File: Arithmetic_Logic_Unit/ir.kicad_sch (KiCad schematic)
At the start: 19 parts, among them IC1 SN54173J, IC2 SN54173J, U1 74LS245

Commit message: added instructional register
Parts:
- removed D1, D2, D3, D4, D5, D6, D7, D8: LED, symbol Device:LED
- removed IC1, IC2: SN54173J, footprints:SN54173J, symbol SN54173J:SN54173J
- removed R1, R2, R3, R4, R5, R6, R7, R8: 220, symbol Device:R
- removed U1: 74LS245, symbol 74xx:74LS245
- added D25, D26, D27, D28, D29, D30, D31, D32: LED, symbol Device:LED
- added IC5, IC6: SN54173J, footprints:SN54173J, symbol SN54173J:SN54173J
- added R25, R26, R27, R28, R29, R30, R31, R32: 220, symbol Device:R
- added U8: 74LS245, symbol 74xx:74LS245
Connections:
- net 5V: now also IC5.16 (VCC), IC6.16 (VCC), U8.1 (A->B), U8.20 (VCC)
- net GND: now also IC5.8 (GND), IC6.8 (GND), R25.2, R26.2, R27.2, R28.2, R29.2, R30.2, R31.2, R32.2, U8.10 (GND)
- net bus0: now also IC5.14 (1D), U8.18 (B0)
- net bus1: now also IC5.13 (2D), U8.17 (B1)
- net bus2: now also IC5.12 (3D), U8.16 (B2)
- net bus3: now also IC5.11 (4D), U8.15 (B3)
- net bus4: now also IC6.14 (1D), U8.14 (B4)
- net bus5: now also IC6.13 (2D), U8.13 (B5)
- net bus6: now also IC6.12 (3D), U8.12 (B6)
- net bus7: now also IC6.11 (4D), U8.11 (B7)
- net clear: now also IC5.15 (CLR), IC6.15 (CLR)
- net clock: now also IC5.7 (CLK), IC6.7 (CLK)
- net enable: now also IC5.1 (M), IC5.2 (N), IC6.1 (M), IC6.2 (N)
- net load: now also IC5.10 (~{G2}), IC5.9 (~{G1}), IC6.10 (~{G2}), IC6.9 (~{G1})
- net q0: now also D25.2 (A), IC5.3 (1Q)
- net q1: now also D26.2 (A), IC5.4 (2Q)
- net q2: now also D27.2 (A), IC5.5 (3Q)
- net q3: now also D28.2 (A), IC5.6 (4Q)
- net q4: now also D29.2 (A), IC6.3 (1Q), U8.6 (A4)
- net q5: now also D30.2 (A), IC6.4 (2Q), U8.7 (A5)
- net q6: now also D31.2 (A), IC6.5 (3Q), U8.8 (A6)
- net q7: now also D32.2 (A), IC6.6 (4Q), U8.9 (A7)
- net ~{OE}: now also U8.19 (CE)
- new net: D29.1 (K), R29.1
- new net: D32.1 (K), R32.1
- new net: D30.1 (K), R30.1
- new net: D28.1 (K), R28.1
- new net: D27.1 (K), R27.1
- new net: D25.1 (K), R25.1
- new net: D26.1 (K), R26.1
- new net: D31.1 (K), R31.1
- no-connect marks 0 -> 4
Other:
- title: Registers -> (none)

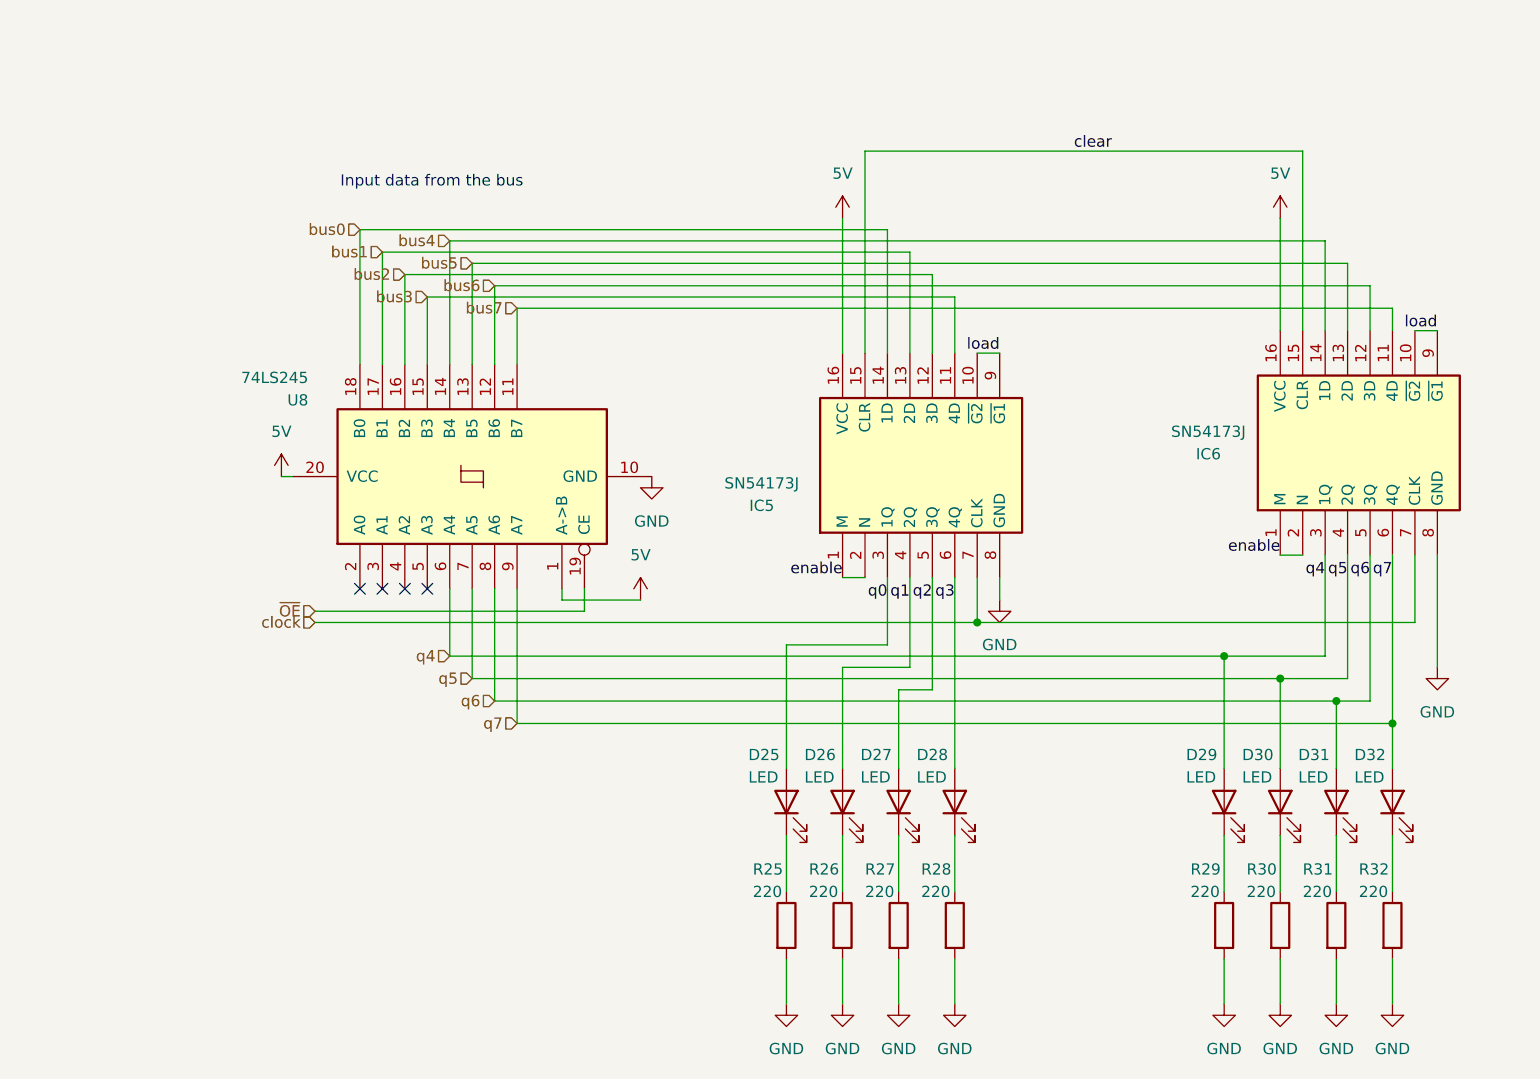
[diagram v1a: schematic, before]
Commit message: fixed incorrect footprint for sn54173
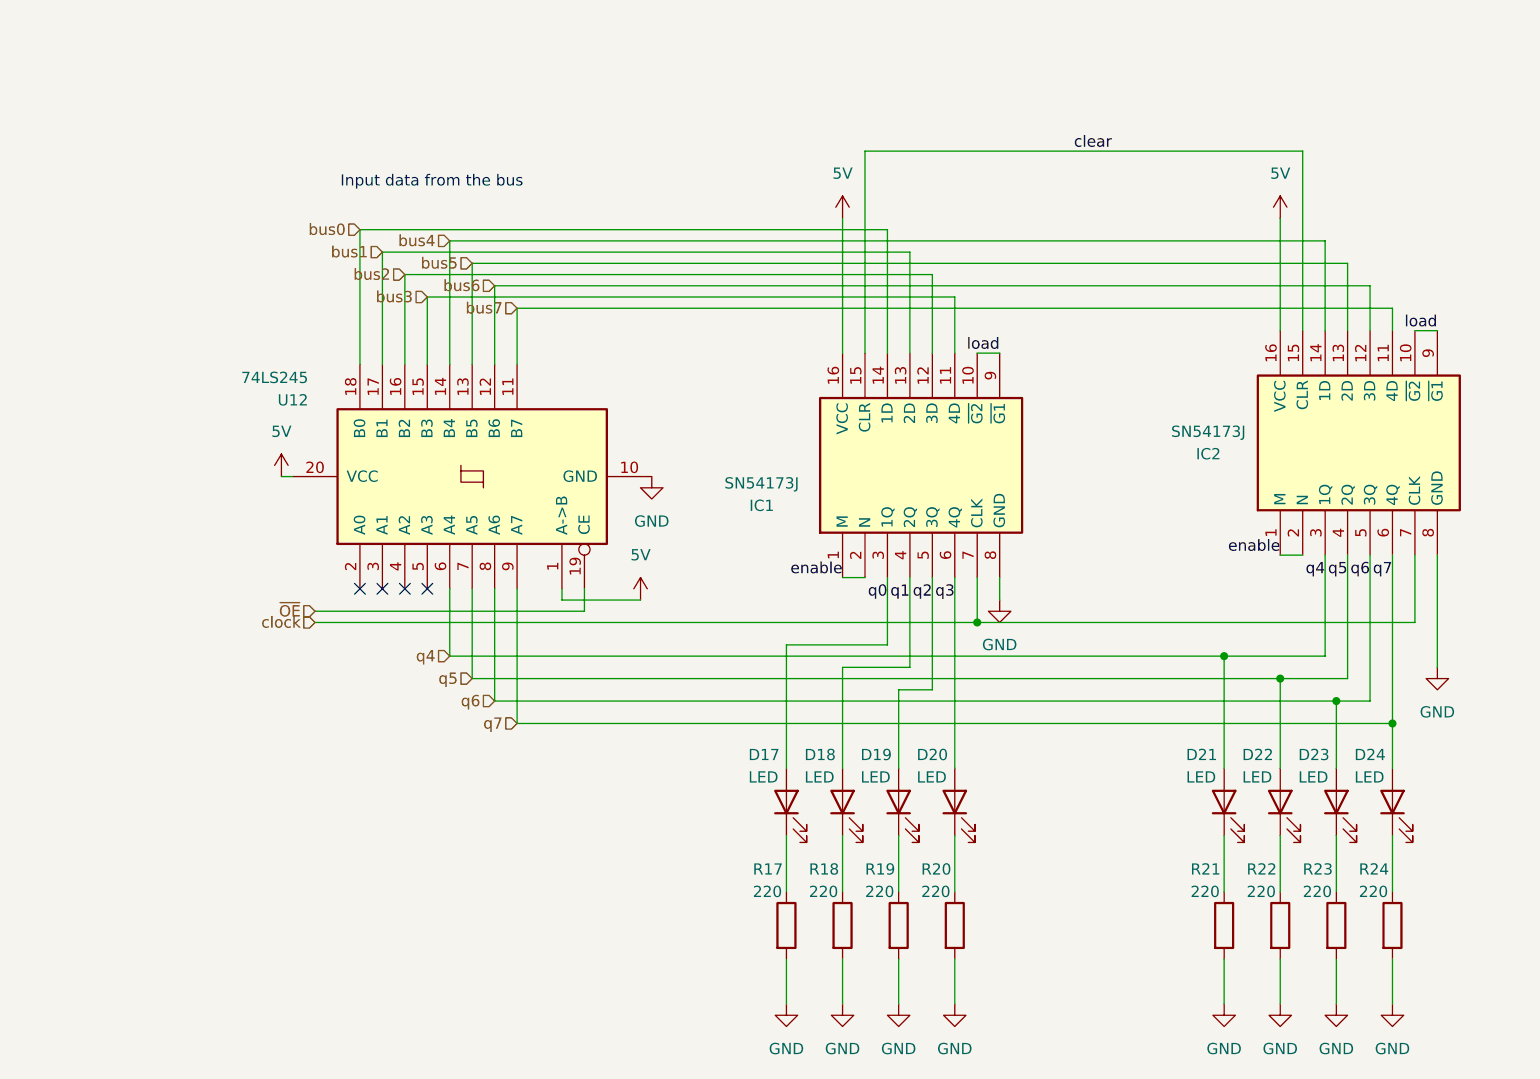
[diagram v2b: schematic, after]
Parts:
- renumbered D25 to D17, D26 to D18, D27 to D19, D28 to D20, D29 to D21, D30 to D22, D31 to D23, D32 to D24, IC5 to IC1, IC6 to IC2, R25 to R17, R26 to R18, R27 to R19, R28 to R20, R29 to R21, R30 to R22, R31 to R23, R32 to R24, U8 to U12

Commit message: added bypass capacitors
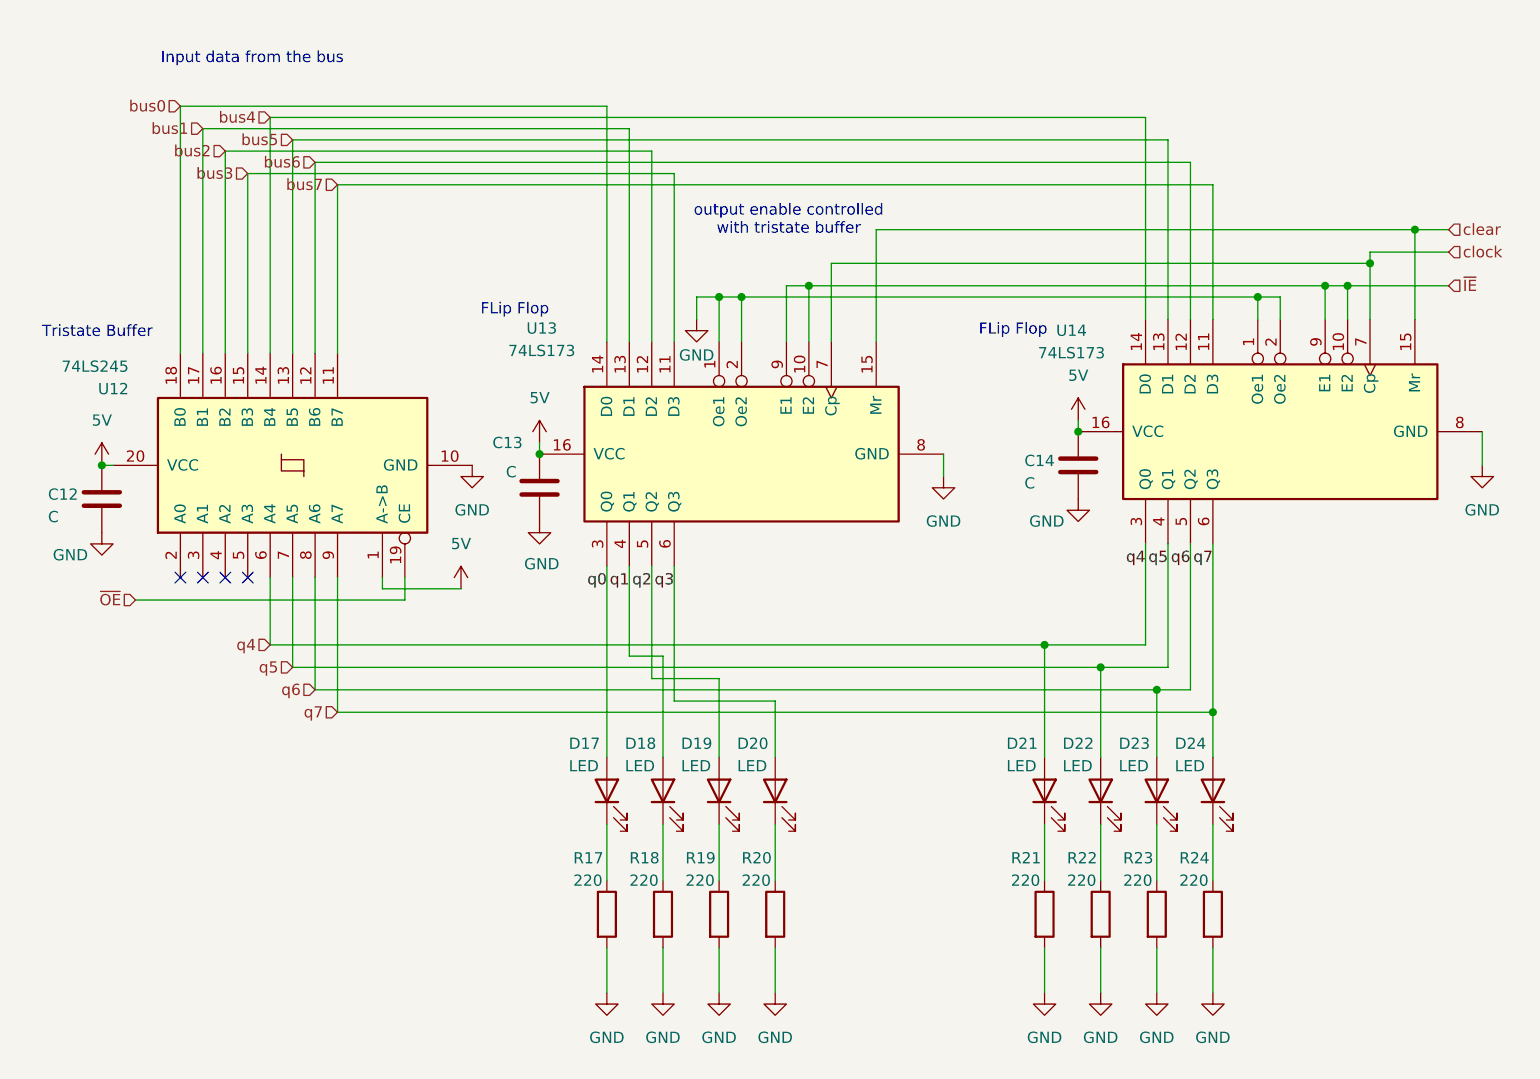
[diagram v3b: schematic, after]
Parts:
- removed IC1, IC2: SN54173J, footprints:SN54173J, symbol SN54173J:SN54173J
- added C12, C13, C14: C, symbol Device:C
- added U13, U14: 74LS173, symbol 74xx:74LS173
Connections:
- net 5V: now also C12.2, C13.2, C14.2, U13.16 (VCC), U14.16 (VCC)
- net GND: now also C12.1, C13.1, C14.1, U13.1 (Oe1), U13.2 (Oe2), U13.8 (GND), U14.1 (Oe1), U14.2 (Oe2), U14.8 (GND)
- net bus0: now also U13.14 (D0)
- net bus1: now also U13.13 (D1)
- net bus2: now also U13.12 (D2)
- net bus3: now also U13.11 (D3)
- net bus4: now also U14.14 (D0)
- net bus5: now also U14.13 (D1)
- net bus6: now also U14.12 (D2)
- net bus7: now also U14.11 (D3)
- net clear: now also U13.15 (Mr), U14.15 (Mr)
- net clock: now also U13.7 (Cp), U14.7 (Cp)
- net q0: now also U13.3 (Q0)
- net q1: now also U13.4 (Q1)
- net q2: now also U13.5 (Q2)
- net q3: now also U13.6 (Q3)
- net q4: now also U14.3 (Q0)
- net q5: now also U14.4 (Q1)
- net q6: now also U14.5 (Q2)
- net q7: now also U14.6 (Q3)
- new net ~{IE}: U13.10 (E2), U13.9 (E1), U14.10 (E2), U14.9 (E1)
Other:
- note added: "FLip Flop"
- note added: "Tristate Buffer"
- note added: "output enable controlled with tristate buffer"

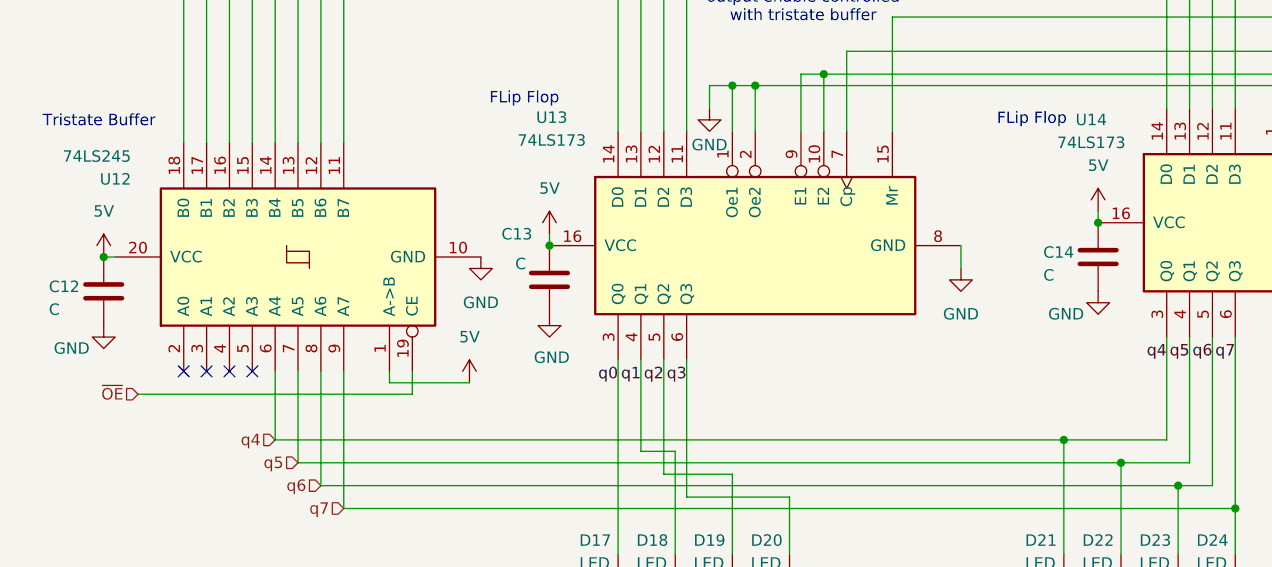
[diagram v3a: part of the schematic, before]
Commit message: preliminary board layout, will move IR to clock module
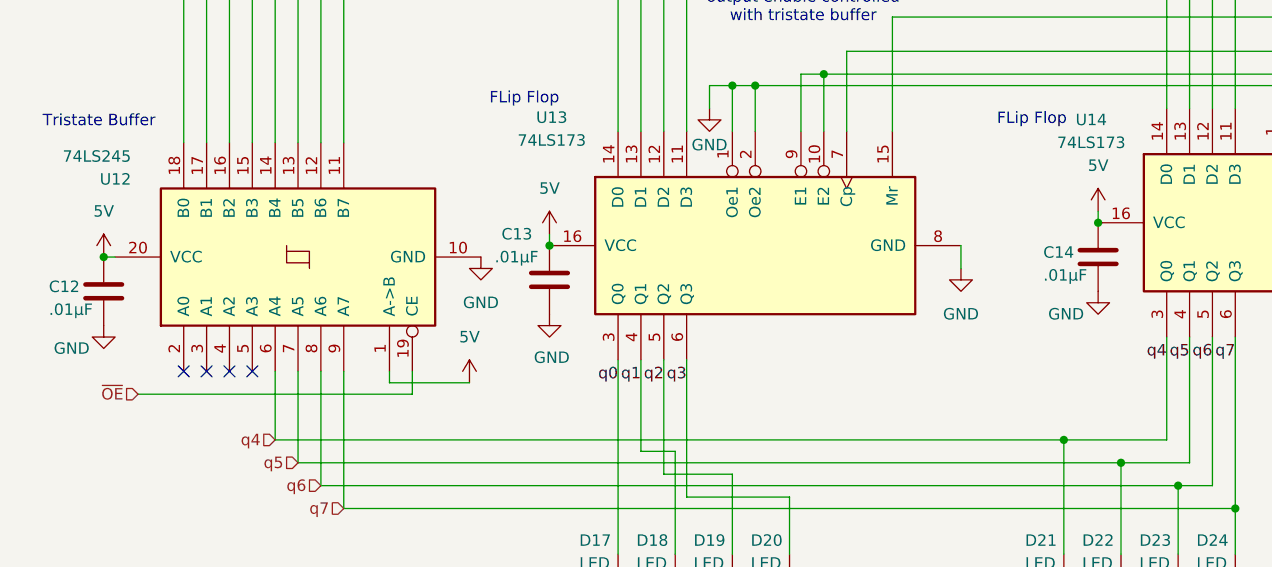
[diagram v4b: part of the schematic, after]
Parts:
- C12, C13, C14: value C -> .01µF; footprint (none) -> Capacitor_THT:C_Disc_D5.0mm_W2.5mm_P2.50mm
- D17, D18, D19, D20, D21, D22, D23, D24: footprint (none) -> LED_THT:LED_D5.0mm
- R17, R18, R19, R20, R21, R22, R23, R24: footprint (none) -> Resistor_THT:R_Axial_DIN0207_L6.3mm_D2.5mm_P5.08mm_Vertical
- U12: footprint (none) -> Package_DIP:DIP-20_W7.62mm
- U13, U14: footprint (none) -> Package_DIP:DIP-16_W7.62mm
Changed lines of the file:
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@@
 			)
 		)
-		(property "Footprint" ""
+		(property "Footprint" "Resistor_THT:R_Axial_DIN0207_L6.3mm_D2.5mm_P5.08mm_Vertical"
 			(at 151.892 123.19 90)
 			(effects
@@
 			)
 		)
-		(property "Footprint" ""
+		(property "Footprint" "Package_DIP:DIP-16_W7.62mm"
 			(at 167.64 68.58 0)
 			(effects
@@
 			)
 		)
-		(property "Footprint" ""
+		(property "Footprint" "Package_DIP:DIP-16_W7.62mm"
 			(at 106.68 71.12 0)
 			(effects
@@
 			)
 		)
-		(property "Value" "C"
+		(property "Value" ".01µF"
 			(at 28.194 78.232 0)
 			(effects
@@
 			)
 		)
-		(property "Footprint" ""
+		(property "Footprint" "Capacitor_THT:C_Disc_D5.0mm_W2.5mm_P2.50mm"
 			(at 33.3248 72.39 0)
 			(effects
@@
 			)
 		)
-		(property "Footprint" ""
+		(property "Footprint" "Resistor_THT:R_Axial_DIN0207_L6.3mm_D2.5mm_P5.08mm_Vertical"
 			(at 139.192 123.19 90)
 			(effects
@@
 			)
 		)
-		(property "Value" "C"
+		(property "Value" ".01µF"
 			(at 138.684 74.422 0)
 			(effects
@@
 			)
 		)
-		(property "Footprint" ""
+		(property "Footprint" "Capacitor_THT:C_Disc_D5.0mm_W2.5mm_P2.50mm"
 			(at 143.8148 68.58 0)
 			(effects
@@
 			)
 		)
-		(property "Footprint" ""
+		(property "Footprint" "LED_THT:LED_D5.0mm"
 			(at 147.32 109.22 0)
 			(effects
@@
 			)
 		)
-		(property "Footprint" ""
+		(property "Footprint" "LED_THT:LED_D5.0mm"
 			(at 104.14 109.22 0)
 			(effects
@@
 			)
 		)
-		(property "Footprint" ""
+		(property "Footprint" "LED_THT:LED_D5.0mm"
 			(at 110.49 109.22 0)
 			(effects
@@
 			)
 		)
-		(property "Footprint" ""
+		(property "Footprint" "Resistor_THT:R_Axial_DIN0207_L6.3mm_D2.5mm_P5.08mm_Vertical"
 			(at 102.362 123.19 90)
 			(effects
@@
 			)
 		)
-		(property "Footprint" ""
+		(property "Footprint" "Resistor_THT:R_Axial_DIN0207_L6.3mm_D2.5mm_P5.08mm_Vertical"
 			(at 108.712 123.19 90)
 			(effects
@@
 			)
 		)
-		(property "Footprint" ""
+		(property "Footprint" "LED_THT:LED_D5.0mm"
 			(at 91.44 109.22 0)
 			(effects
@@
 			)
 		)
-		(property "Footprint" ""
+		(property "Footprint" "LED_THT:LED_D5.0mm"
 			(at 153.67 109.22 0)
 			(effects
@@
 			)
 		)
-		(property "Footprint" ""
+		(property "Footprint" "Resistor_THT:R_Axial_DIN0207_L6.3mm_D2.5mm_P5.08mm_Vertical"
 			(at 96.012 123.19 90)
 			(effects
@@
 			)
 		)
-		(property "Footprint" ""
+		(property "Footprint" "LED_THT:LED_D5.0mm"
 			(at 97.79 109.22 0)
 			(effects
@@
 			)
 		)
-		(property "Footprint" ""
+		(property "Footprint" "Resistor_THT:R_Axial_DIN0207_L6.3mm_D2.5mm_P5.08mm_Vertical"
 			(at 145.542 123.19 90)
 			(effects
@@
 			)
 		)
-		(property "Footprint" ""
+		(property "Footprint" "Package_DIP:DIP-20_W7.62mm"
 			(at 55.88 72.39 0)
 			(effects
@@
 			)
 		)
-		(property "Footprint" ""
+		(property "Footprint" "LED_THT:LED_D5.0mm"
 			(at 140.97 109.22 0)
 			(effects
@@
 			)
 		)
-		(property "Footprint" ""
+		(property "Footprint" "Resistor_THT:R_Axial_DIN0207_L6.3mm_D2.5mm_P5.08mm_Vertical"
 			(at 89.662 123.19 90)
 			(effects
@@
 			)
 		)
-		(property "Footprint" ""
+		(property "Footprint" "Resistor_THT:R_Axial_DIN0207_L6.3mm_D2.5mm_P5.08mm_Vertical"
 			(at 158.242 123.19 90)
 			(effects
@@
 			)
 		)
-		(property "Value" "C"
-			(at 80.01 73.152 0)
+		(property "Value" ".01µF"
+			(at 77.724 72.39 0)
 			(effects
 				(font
@@
 			)
 		)
-		(property "Footprint" ""
+		(property "Footprint" "Capacitor_THT:C_Disc_D5.0mm_W2.5mm_P2.50mm"
 			(at 82.8548 71.12 0)
 			(effects
@@
 			)
 		)
-		(property "Footprint" ""
+		(property "Footprint" "LED_THT:LED_D5.0mm"
 			(at 160.02 109.22 0)
 			(effects
